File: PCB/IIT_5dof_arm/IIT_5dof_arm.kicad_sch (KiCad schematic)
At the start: 46 parts, among them J1 Screw_Terminal_01x02, J14 Conn_02x13_Top_Bottom, J8 Conn_01x04, SW1 SW_MAIN, SW15 SW_MOT, SW17 SW_SPDT, SW18 SW_SPDT, SW19 SW_SPDT, SW20 SW_SPDT, SW21 SW_SPDT, SW22 SW_SPDT, SW23 SW_SPDT, SW24 SW_SPDT, SW25 SW_SPDT, SW26 SW_SPDT, SW27 SW_SPDT, SW28 SW_SPDT, U5 XL8574T, U7 SN74LV1T34DBV, U8 SN74LV1T34DBV, U9 4504

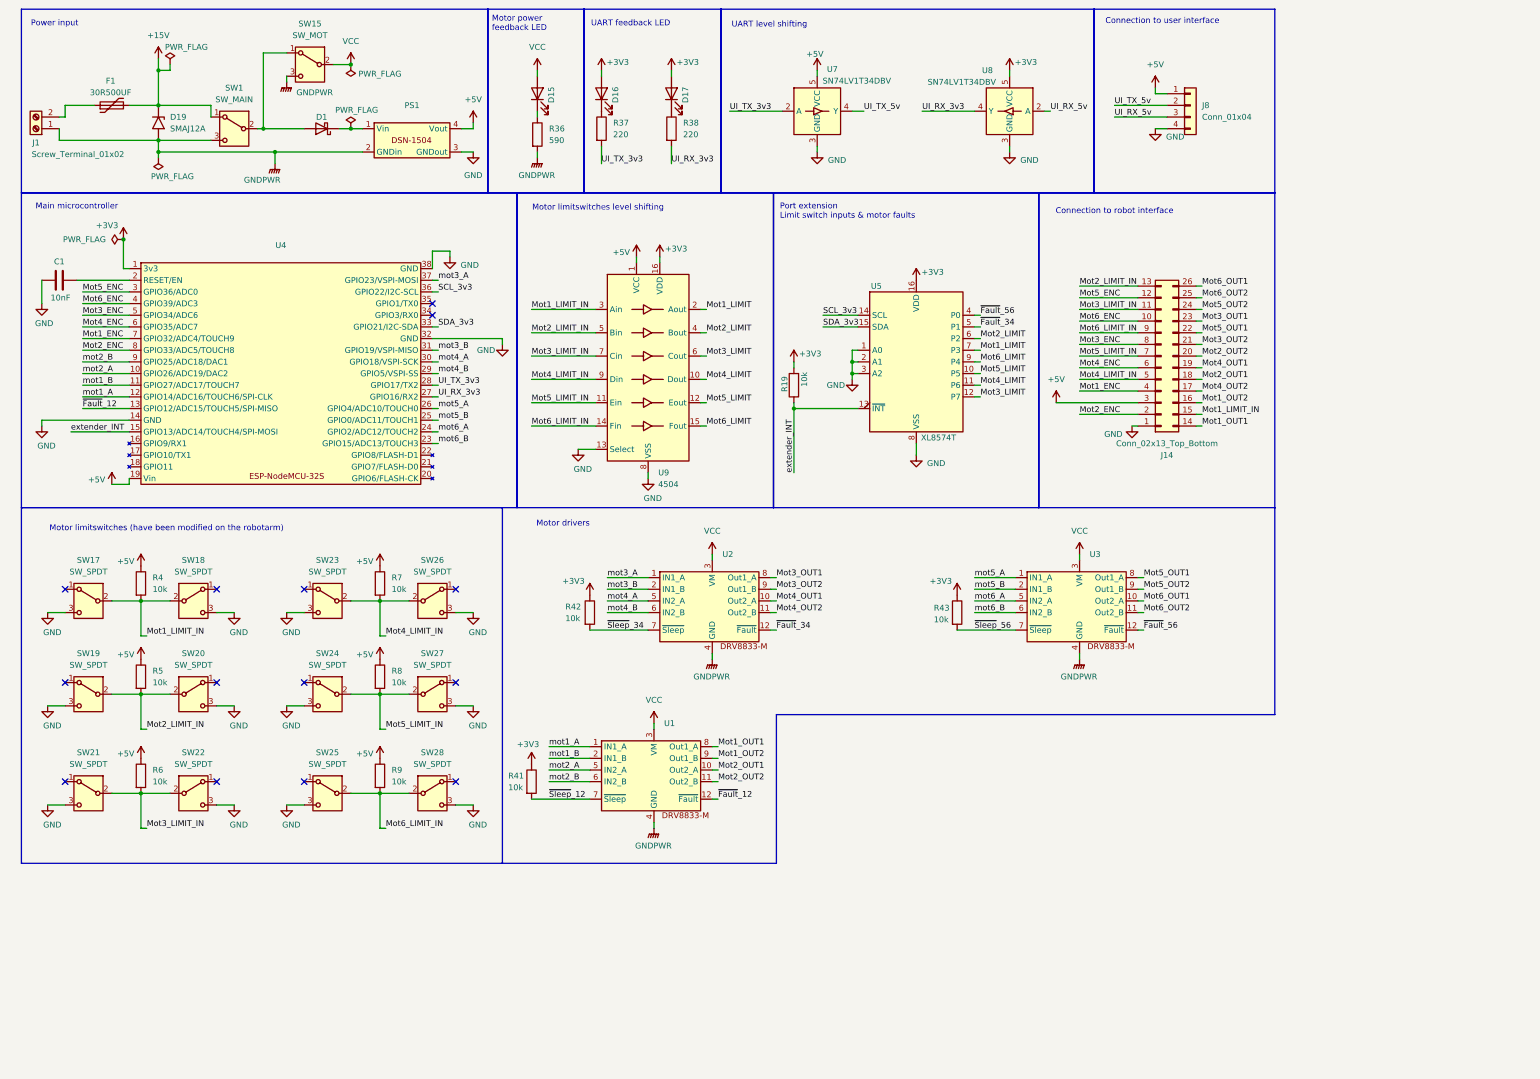
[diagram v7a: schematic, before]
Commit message: implement RS232
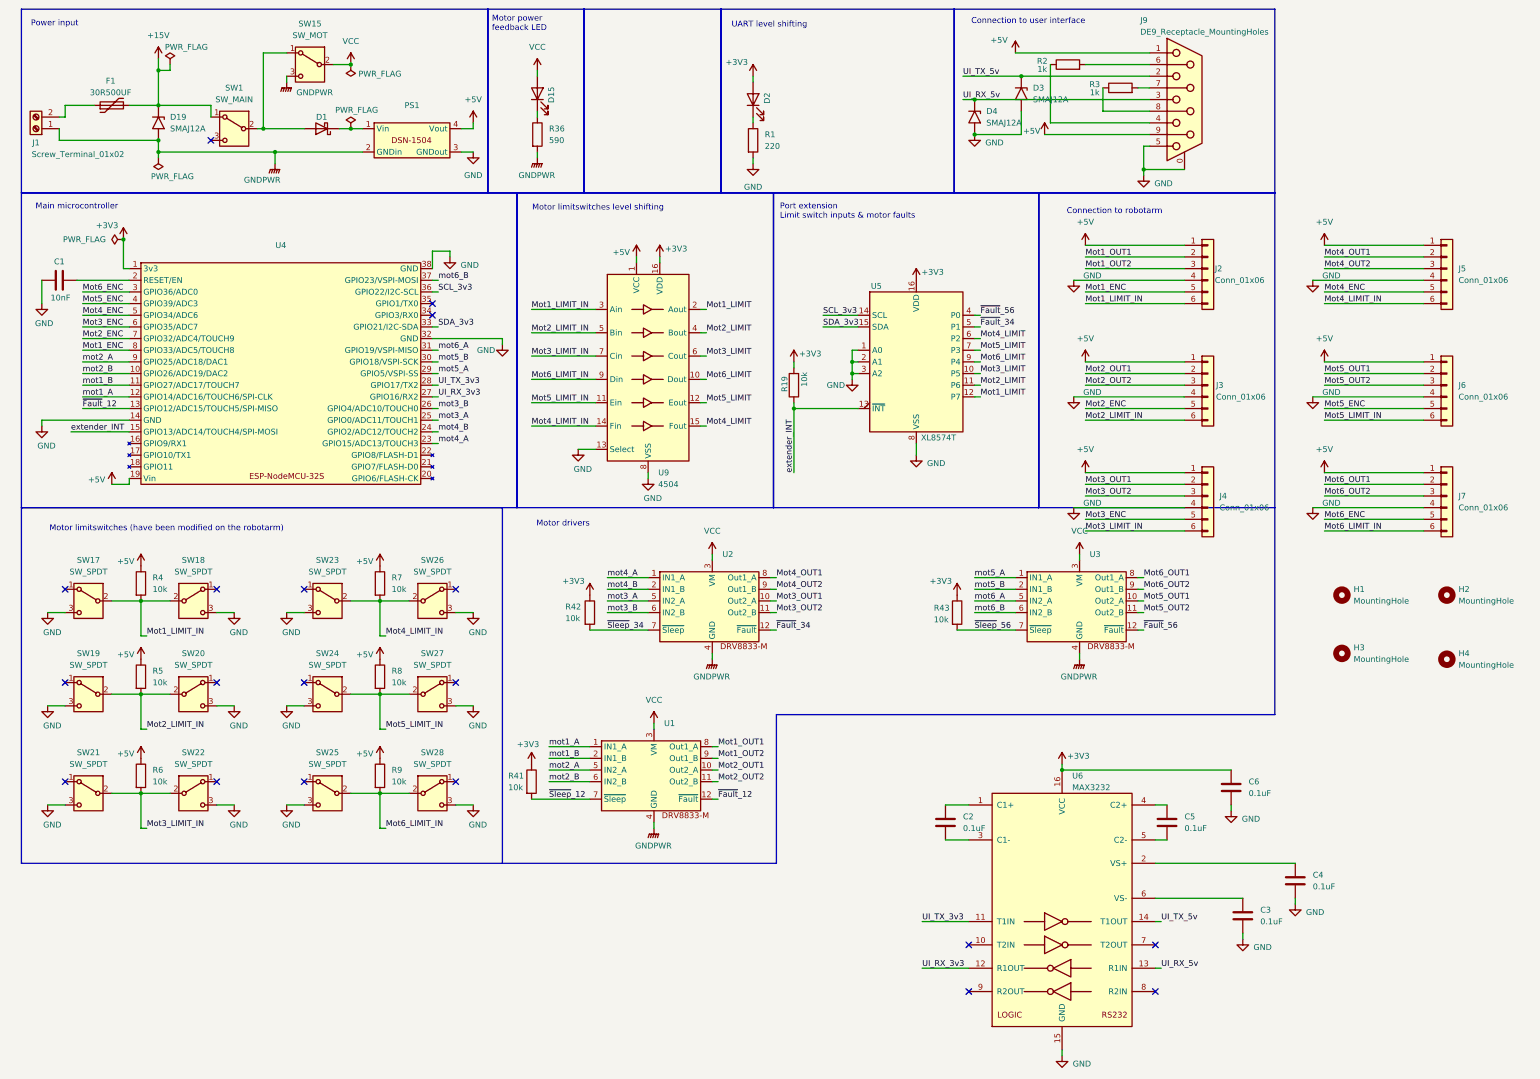
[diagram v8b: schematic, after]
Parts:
- removed D16, D17: LED, LED_SMD:LED_0805_2012Metric_Pad1.15x1.40mm_HandSolder, symbol Device:LED
- removed J14: Conn_02x13_Top_Bottom, Connector_IDC:IDC-Header_2x13_P2.54mm_Vertical, symbol Connector_Generic:Conn_02x13_Top_Bottom
- removed J8: Conn_01x04, Connector_Molex:Molex_KK-254_AE-6410-04A_1x04_P2.54mm_Vertical, symbol Connector_Generic:Conn_01x04
- removed R37, R38: 220, Resistor_SMD:R_0805_2012Metric_Pad1.20x1.40mm_HandSolder, symbol Device:R
- removed U7, U8: SN74LV1T34DBV, Package_TO_SOT_SMD:SOT-23-5_HandSoldering, symbol Logic_LevelTranslator:SN74LV1T34DBV
- added C2, C3, C4, C5, C6: 0.1uF, Capacitor_SMD:C_0805_2012Metric_Pad1.18x1.45mm_HandSolder, symbol Device:C
- added D2: LED, Connector_Molex:Molex_KK-254_AE-6410-02A_1x02_P2.54mm_Vertical, symbol Device:LED
- added D3, D4: SMAJ12A, Diode_SMD:D_SMA_Handsoldering, symbol Diode:SMAJ12A
- added H1, H2, H3, H4: MountingHole, MountingHole:MountingHole_3.2mm_M3, symbol Mechanical:MountingHole
- added J2, J3, J4, J5, J6, J7: Conn_01x06, Connector_Molex:Molex_KK-254_AE-6410-06A_1x06_P2.54mm_Vertical, symbol Connector_Generic:Conn_01x06
- added J9: DE9_Receptacle_MountingHoles, Connector_Dsub:DSUB-9_Female_Horizontal_P2.77x2.84mm_EdgePinOffset4.94mm_Housed_MountingHolesOffset7.48mm, symbol Connector:DE9_Receptacle_MountingHoles
- added R1: 220, Resistor_SMD:R_0805_2012Metric_Pad1.20x1.40mm_HandSolder, symbol Device:R
- added R2, R3: 1k, Resistor_SMD:R_0805_2012Metric_Pad1.20x1.40mm_HandSolder, symbol Device:R
- added U6: MAX3232, Package_SO:SOIC-16W_5.3x10.2mm_P1.27mm, symbol Interface_UART:MAX3232
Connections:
- net +3V3: now also C6.1, D2.2 (A), U6.16 (VCC)
- net +5V: now also J2.1 (Pin_1), J3.1 (Pin_1), J4.1 (Pin_1), J5.1 (Pin_1), J6.1 (Pin_1), J7.1 (Pin_1), J9.1, J9.9
- net GND: now also C3.2, C4.2, C6.2, D3.2 (A2), D4.2 (A2), J2.4 (Pin_4), J3.4 (Pin_4), J4.4 (Pin_4), J5.4 (Pin_4), J6.4 (Pin_4), J7.4 (Pin_4), J9.0 (PAD), J9.5, R1.2, U6.15 (GND)
- net GNDPWR: no longer SW1.3 (C)
- net Mot1_ENC: now also U4.8 (GPIO33/ADC5/TOUCH8), J2.5 (Pin_5); no longer U4.7 (GPIO32/ADC4/TOUCH9)
- net Mot1_LIMIT: now also U5.12 (P7); no longer U5.7 (P3)
- net Mot1_LIMIT_IN: now also J2.6 (Pin_6)
- net Mot1_OUT1: now also J2.2 (Pin_2)
- net Mot1_OUT2: now also J2.3 (Pin_3)
- net Mot2_ENC: now also U4.7 (GPIO32/ADC4/TOUCH9), J3.5 (Pin_5); no longer U4.8 (GPIO33/ADC5/TOUCH8)
- net Mot2_LIMIT: now also U5.11 (P6); no longer U5.6 (P2)
- net Mot2_LIMIT_IN: now also J3.6 (Pin_6)
- net Mot2_OUT1: now also J3.2 (Pin_2)
- net Mot2_OUT2: now also J3.3 (Pin_3)
- net Mot3_ENC: now also U4.6 (GPIO35/ADC7), J4.5 (Pin_5); no longer U4.5 (GPIO34/ADC6)
- net Mot3_LIMIT: now also U5.10 (P5); no longer U5.12 (P7)
- net Mot3_LIMIT_IN: now also J4.6 (Pin_6)
- net Mot3_OUT1: now also U2.10 (Out2_A), J4.2 (Pin_2); no longer U2.8 (Out1_A)
- net Mot3_OUT2: now also U2.11 (Out2_B), J4.3 (Pin_3); no longer U2.9 (Out1_B)
- net Mot4_ENC: now also U4.5 (GPIO34/ADC6), J5.5 (Pin_5); no longer U4.6 (GPIO35/ADC7)
- net Mot4_LIMIT: now also U5.6 (P2), U9.15 (Fout); no longer U5.11 (P6), U9.10 (Dout)
- net Mot4_LIMIT_IN: now also U9.14 (Fin), J5.6 (Pin_6); no longer U9.9 (Din)
- net Mot4_OUT1: now also U2.8 (Out1_A), J5.2 (Pin_2); no longer U2.10 (Out2_A)
- net Mot4_OUT2: now also U2.9 (Out1_B), J5.3 (Pin_3); no longer U2.11 (Out2_B)
- net Mot5_ENC: now also U4.4 (GPIO39/ADC3), J6.5 (Pin_5); no longer U4.3 (GPIO36/ADC0)
- net Mot5_LIMIT: now also U5.7 (P3); no longer U5.10 (P5)
- net Mot5_LIMIT_IN: now also J6.6 (Pin_6)
- net Mot5_OUT1: now also U3.10 (Out2_A), J6.2 (Pin_2); no longer U3.8 (Out1_A)
- net Mot5_OUT2: now also U3.11 (Out2_B), J6.3 (Pin_3); no longer U3.9 (Out1_B)
- net Mot6_ENC: now also U4.3 (GPIO36/ADC0), J7.5 (Pin_5); no longer U4.4 (GPIO39/ADC3)
- net Mot6_LIMIT: now also U9.10 (Dout); no longer U9.15 (Fout)
- net Mot6_LIMIT_IN: now also U9.9 (Din), J7.6 (Pin_6); no longer U9.14 (Fin)
- net Mot6_OUT1: now also U3.8 (Out1_A), J7.2 (Pin_2); no longer U3.10 (Out2_A)
- net Mot6_OUT2: now also U3.9 (Out1_B), J7.3 (Pin_3); no longer U3.11 (Out2_B)
- net UI_RX_3v3: now also U6.12 (R1OUT)
- net UI_RX_5v: now also D4.1 (A1), J9.3, U6.13 (R1IN)
- net UI_TX_3v3: now also U6.11 (T1IN)
- net UI_TX_5v: now also D3.1 (A1), J9.2, U6.14 (T1OUT)
- net mot2_A: now also U4.9 (GPIO25/ADC18/DAC1); no longer U4.10 (GPIO26/ADC19/DAC2)
- net mot2_B: now also U4.10 (GPIO26/ADC19/DAC2); no longer U4.9 (GPIO25/ADC18/DAC1)
- net mot3_A: now also U2.5 (IN2_A), U4.25 (GPIO0/ADC11/TOUCH1); no longer U2.1 (IN1_A), U4.37 (GPIO23/VSPI-MOSI)
- net mot3_B: now also U2.6 (IN2_B), U4.26 (GPIO4/ADC10/TOUCH0); no longer U2.2 (IN1_B), U4.31 (GPIO19/VSPI-MISO)
- net mot4_A: now also U2.1 (IN1_A), U4.23 (GPIO15/ADC13/TOUCH3); no longer U2.5 (IN2_A), U4.30 (GPIO18/VSPI-SCK)
- net mot4_B: now also U2.2 (IN1_B), U4.24 (GPIO2/ADC12/TOUCH2); no longer U2.6 (IN2_B), U4.29 (GPIO5/VSPI-SS)
- net mot5_A: now also U4.29 (GPIO5/VSPI-SS); no longer U4.26 (GPIO4/ADC10/TOUCH0)
- net mot5_B: now also U4.30 (GPIO18/VSPI-SCK); no longer U4.25 (GPIO0/ADC11/TOUCH1)
- net mot6_A: now also U4.31 (GPIO19/VSPI-MISO); no longer U4.24 (GPIO2/ADC12/TOUCH2)
- net mot6_B: now also U4.37 (GPIO23/VSPI-MOSI); no longer U4.23 (GPIO15/ADC13/TOUCH3)
- new net: C2.1, U6.1 (C1+)
- new net: C2.2, U6.3 (C1-)
- new net: C4.1, U6.2 (VS+)
- new net: C5.1, U6.4 (C2+)
- new net: C5.2, U6.5 (C2-)
- new net: C3.1, U6.6 (VS-)
- new net: J9.4, R2.1
- new net: J9.6, R2.2
- new net: J9.7, R3.2
- new net: J9.8, R3.1
- new net: D2.1 (K), R1.1
- no-connect marks 14 -> 19
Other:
- note added: "Connection to robotarm"
- note removed: "Connection to robot interface"
- note removed: "UART feedback LED"
